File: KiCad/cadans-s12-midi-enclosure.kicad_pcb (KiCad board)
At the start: 2 copper layers, 256.3 x 79.4 mm, 0 parts

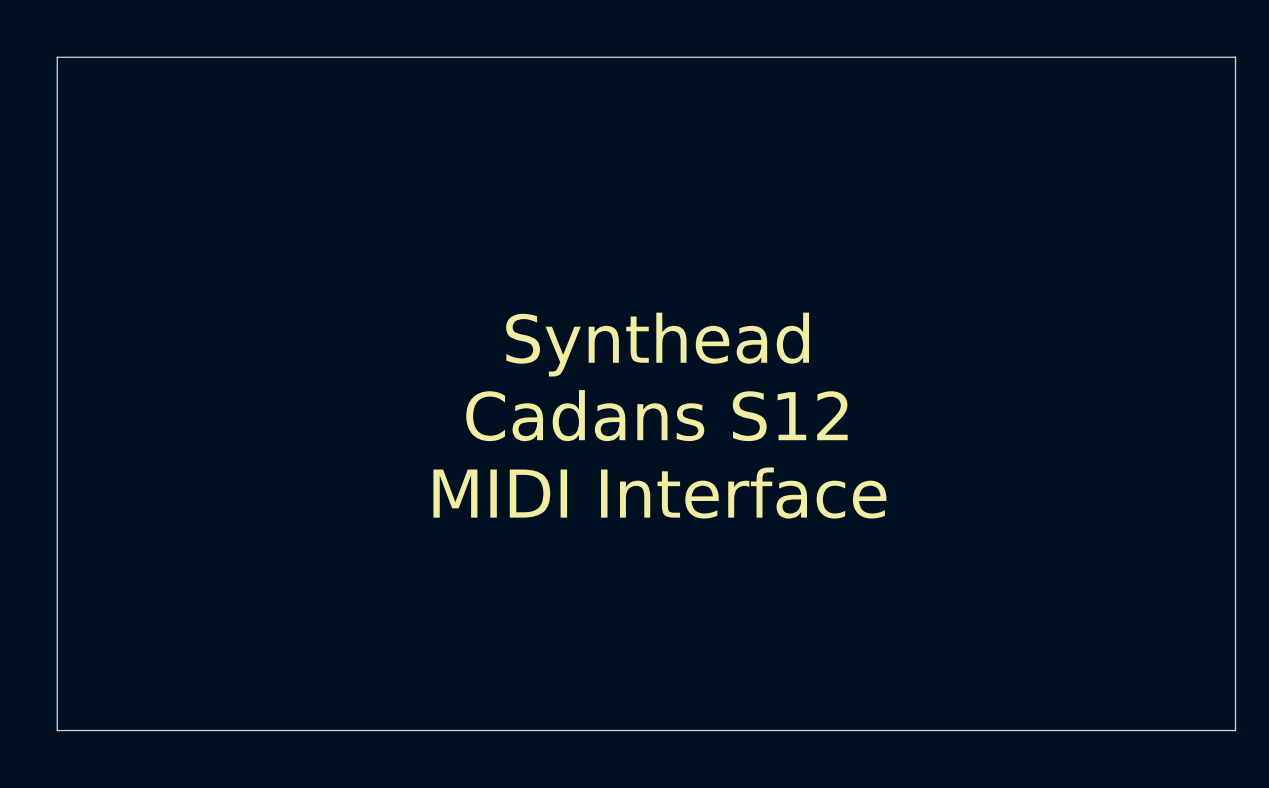
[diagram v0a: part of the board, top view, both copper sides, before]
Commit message: Center top enclosure text.
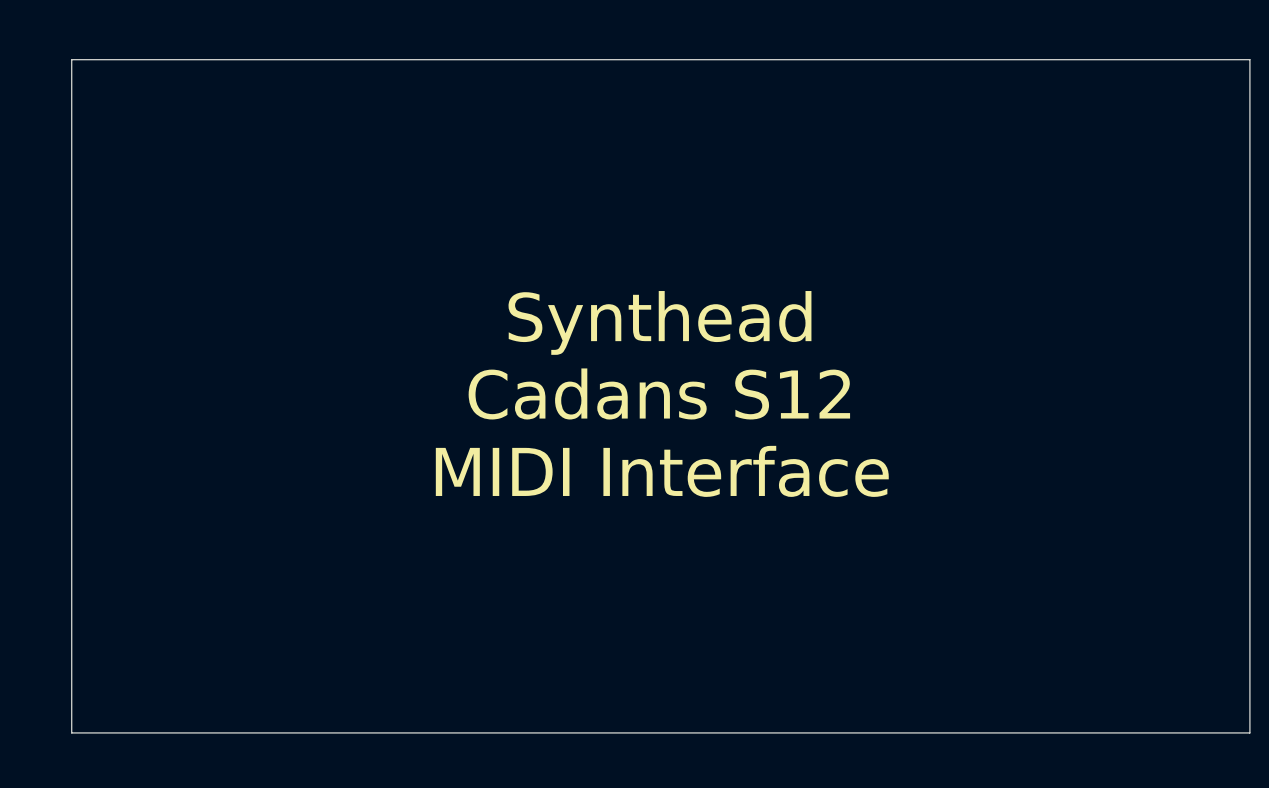
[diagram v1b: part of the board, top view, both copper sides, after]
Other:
- board size 256.3 x 79.4 mm -> 257.8 x 79.4 mm
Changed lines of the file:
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@@
     (uvia_drill 0.1)
   )
-  (gr_line (start 150.876 134.366) (end 150.876 63.246) (layer Edge.Cuts) (width 0.1))
-  (gr_line (start 275.336 134.366) (end 150.876 134.366) (layer Edge.Cuts) (width 0.1))
-  (gr_text "Synthead\nCadans S12\nMIDI Interface" (at 214.376 101.346) (layer F.SilkS)
+  (gr_line (start 152.4 134.62) (end 152.4 63.5) (layer Edge.Cuts) (width 0.1))
+  (gr_line (start 276.86 134.62) (end 152.4 134.62) (layer Edge.Cuts) (width 0.1))
+  (gr_text "Synthead\nCadans S12\nMIDI Interface" (at 214.63 99.06) (layer F.SilkS)
     (effects (font (size 5.08 5.08) (thickness 1.016)))
   )
-  (gr_line (start 275.336 63.246) (end 275.336 134.366) (layer Edge.Cuts) (width 0.1))
-  (gr_line (start 150.876 63.246) (end 275.336 63.246) (layer Edge.Cuts) (width 0.1))
+  (gr_line (start 276.86 63.5) (end 276.86 134.62) (layer Edge.Cuts) (width 0.1))
+  (gr_line (start 152.4 63.5) (end 276.86 63.5) (layer Edge.Cuts) (width 0.1))
   (gr_line (start 91.2495 65.3415) (end 91.2495 62.1665) (layer Dwgs.User) (width 0.15))
   (gr_line (start 122.9995 62.1665) (end 91.2495 62.1665) (layer Dwgs.User) (width 0.15))
